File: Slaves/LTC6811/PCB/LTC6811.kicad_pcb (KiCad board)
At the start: 2 copper layers, 100 x 100 mm, 108 parts, among them J1 Cells, J2 Slave, J3 Master, J4 Temperature, J5 Conn_01x01, J6 Conn_01x01, J7 Conn_01x01, J8 Conn_01x01, Q1 NSV1C201MZ4, Q10 TSM2323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

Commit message: description on PCB
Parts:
- added LOGO1: Logo_Open_Hardware_Small, ENNOID:ENNOID-LOGO, B.Cu at (53.0, 39.0)
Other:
- board text added: "LTC6811"
- board text added: "Slave LTC6811 - 01/2018 https://github.com/EnnoidMe/ENNOID-BMS"

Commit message: UPS update
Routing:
- net Net-(F6-Pad1): track 3.71 -> 9.70 mm
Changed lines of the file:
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@@
     (thickness 1.6)
     (drawings 10)
-    (tracks 666)
+    (tracks 667)
     (zones 0)
     (modules 109)
@@
   (segment (start 29 51.05) (end 30.85 51.05) (width 0.25) (layer F.Cu) (net 36) (status 30))
   (segment (start 5.92 46) (end 3.3 48.62) (width 0.25) (layer F.Cu) (net 37) (status 20))
+  (segment (start 5.92 46) (end 11.91 46) (width 0.25) (layer F.Cu) (net 37))
   (segment (start 4.14 52) (end 3.3 51.16) (width 0.25) (layer F.Cu) (net 38) (status 30))
   (segment (start 11.91 52) (end 4.14 52) (width 0.25) (layer F.Cu) (net 38) (status 30))

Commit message: UPS completed
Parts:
- moved J4 0.82 mm to (67.5, 97.5)
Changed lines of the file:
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@@
     (47 F.CrtYd user)
     (48 B.Fab user)
-    (49 F.Fab user)
+    (49 F.Fab user hide)
   )
   (setup
@@
   )
   (module Pin_Headers:Pin_Header_Straight_1x06_Pitch2.54mm (layer F.Cu)
-    (at 67.3 96.7 90)
+    (at 67.5 97.5 90)
     (descr "Through hole straight pin header, 1x06, 2.54mm pitch, single row")
     (tags "Through hole pin header THT 1x06 2.54mm single row")

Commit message: Software added
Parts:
- C13, C14, C15, C16, C17, C18, C19, C20, C21, C22, C23, C24: footprint Capacitors_SMD:C_0603_HandSoldering -> Capacitors_SMD:C_0805_HandSoldering

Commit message: LTC6811 added diode protection inputs
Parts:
- added D1: PDZ7.5B, Diodes_SMD:D_SOD-323_HandSoldering, F.Cu at (35.9, 23.0)
- added D10: PDZ7.5B, Diodes_SMD:D_SOD-323_HandSoldering, F.Cu at (35.9, 77.0)
- added D11: PDZ7.5B, Diodes_SMD:D_SOD-323_HandSoldering, F.Cu at (35.9, 83.3)
- added D12: PDZ7.5B, Diodes_SMD:D_SOD-323_HandSoldering, F.Cu at (35.9, 89.0)
- added D2: PDZ7.5B, Diodes_SMD:D_SOD-323_HandSoldering, F.Cu at (35.9, 29.0)
- added D3: PDZ7.5B, Diodes_SMD:D_SOD-323_HandSoldering, F.Cu at (35.9, 35.0)
- added D4: PDZ7.5B, Diodes_SMD:D_SOD-323_HandSoldering, F.Cu at (35.9, 41.0)
- added D5: PDZ7.5B, Diodes_SMD:D_SOD-323_HandSoldering, F.Cu at (35.9, 47.0)
- added D6: PDZ7.5B, Diodes_SMD:D_SOD-323_HandSoldering, F.Cu at (35.9, 53.0)
- added D7: PDZ7.5B, Diodes_SMD:D_SOD-323_HandSoldering, F.Cu at (35.9, 59.5)
- added D8: PDZ7.5B, Diodes_SMD:D_SOD-323_HandSoldering, F.Cu at (35.9, 65.5)
- added D9: PDZ7.5B, Diodes_SMD:D_SOD-323_HandSoldering, F.Cu at (35.9, 71.0)
- added F13: 0.25A, Fuse_Holders_and_Fuses:Fuse_SMD1206_HandSoldering, F.Cu at (14.0, 88.0)
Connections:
- J1 pad 1: GND -> Net-(F13-Pad1)
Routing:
- net Net-(F13-Pad1): track 0.00 -> 27.2 mm
- net GND: track 96.2 -> 71.4 mm, vias 27 -> 30
- net /cell6/C: track 18.9 -> 24.1 mm
- net /cell7/C: track 18.1 -> 23.1 mm
- net /cell11/C: track 35.2 -> 40.0 mm
- net /cell5/C: track 21.0 -> 25.7 mm
- net /cell9/C: track 25.9 -> 30.6 mm
- net /cell8/C: track 20.1 -> 24.8 mm
- net /cell10/C: track 30.8 -> 35.3 mm
- net /cell2/C: track 38.3 -> 42.6 mm
- net /cell1/C: track 42.7 -> 46.6 mm
- net /cell3/C: track 31.7 -> 35.2 mm
- net /cell4/C: track 26.9 -> 29.9 mm
- net /cell6/S: track 19.5 -> 21.1 mm
- net /cell12/C: track 40.9 -> 42.0 mm
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
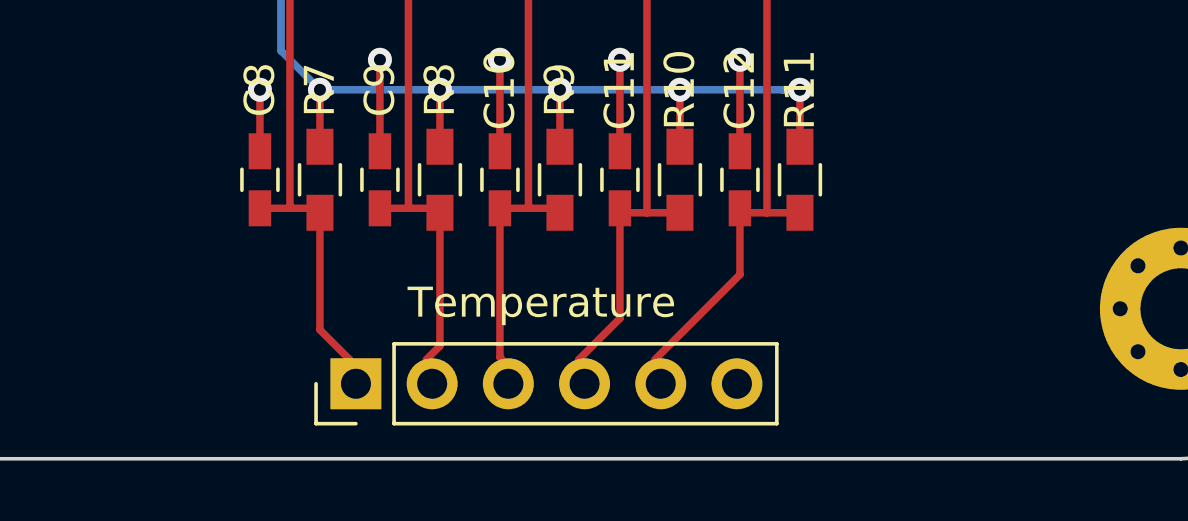
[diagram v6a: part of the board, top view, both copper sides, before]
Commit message: temperatures sensors now has  separate grounds
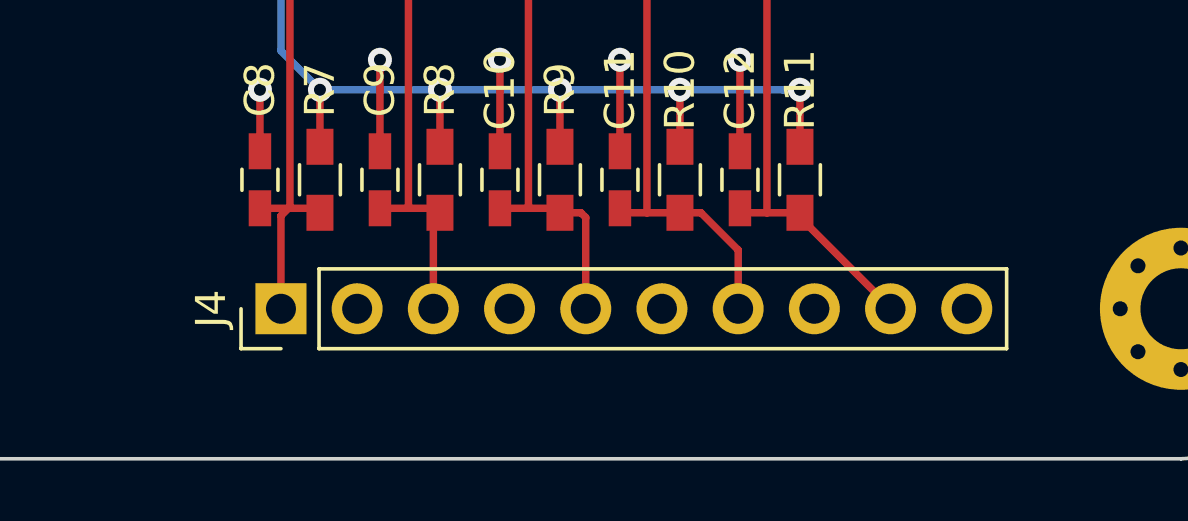
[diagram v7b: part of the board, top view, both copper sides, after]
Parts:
- J4: footprint Pin_Headers:Pin_Header_Straight_1x06_Pitch2.54mm -> Pin_Headers:Pin_Header_Straight_1x10_Pitch2.54mm
- moved J4 3.54 mm to (65.0, 95.0)
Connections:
- J4 pad 2: /T2 -> GND
- J4 pad 3: /T3 -> /T2
- J4 pad 4: /T4 -> GND
- J4 pad 5: /T5 -> /T3
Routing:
- net /T1: track 46.9 -> 45.0 mm
- net /T2: track 49.1 -> 47.3 mm
- net /T5: track 58.2 -> 56.4 mm
- net /T4: track 55.1 -> 53.9 mm
- net /T3: track 51.5 -> 50.4 mm

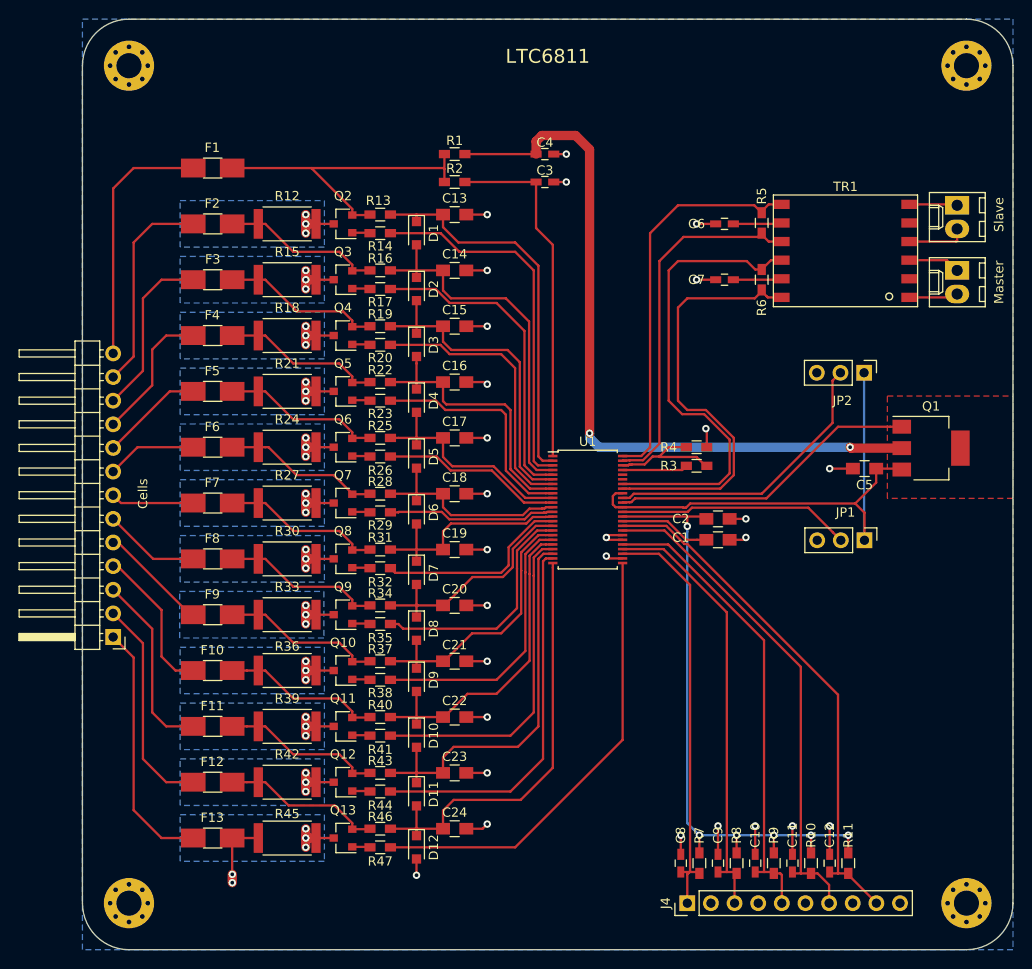
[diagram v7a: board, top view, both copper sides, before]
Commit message: LTC6811 is now 2W per level
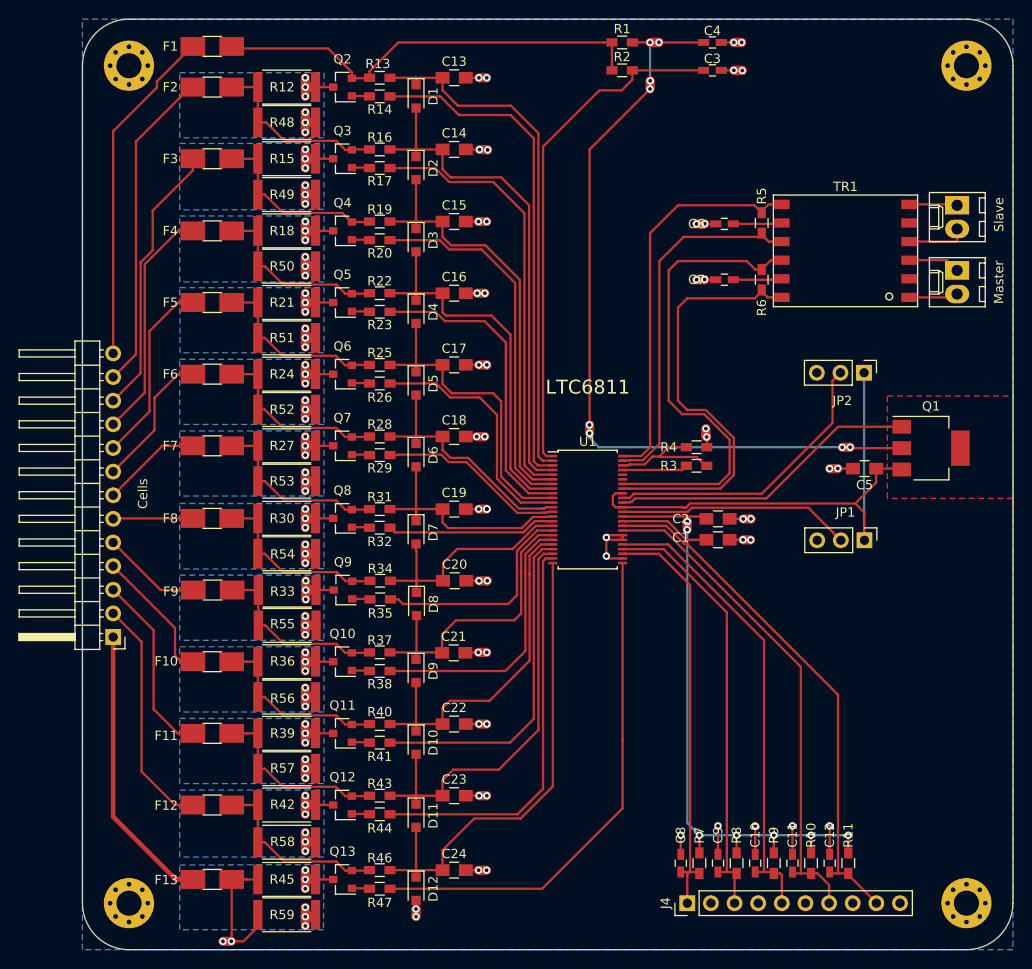
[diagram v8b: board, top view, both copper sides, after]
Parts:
- added R48: 15, Resistors_SMD:R_2512, F.Cu at (21.9, 11.1)
- added R49: 15, Resistors_SMD:R_2512, F.Cu at (21.9, 18.9)
- added R50: 15, Resistors_SMD:R_2512, F.Cu at (21.9, 26.6)
- added R51: 15, Resistors_SMD:R_2512, F.Cu at (21.9, 34.2)
- added R52: 15, Resistors_SMD:R_2512, F.Cu at (21.9, 42.0)
- added R53: 15, Resistors_SMD:R_2512, F.Cu at (21.9, 49.6)
- added R54: 15, Resistors_SMD:R_2512, F.Cu at (21.9, 57.5)
- added R55: 15, Resistors_SMD:R_2512, F.Cu at (22.0, 65.2)
- added R56: 15, Resistors_SMD:R_2512, F.Cu at (21.9, 72.8)
- added R57: 15, Resistors_SMD:R_2512, F.Cu at (21.9, 80.5)
- added R58: 15, Resistors_SMD:R_2512, F.Cu at (21.9, 88.5)
- added R59: 15, Resistors_SMD:R_2512, F.Cu at (21.9, 96.2)
- R12, R15, R18, R21, R24, R27, R30, R33, R36, R39, R42, R45: value 33 -> 15
- moved C3 21.6 mm to (67.7, 5.50)
- moved C4 21.6 mm to (67.7, 2.50)
- moved R1 21.6 mm to (58.0, 2.50)
- moved R2 21.6 mm to (58.0, 5.50)
- moved C13 14.7 mm to (40.0, 6.30)
- moved D1 14.7 mm to (35.9, 8.30)
- moved F2 14.7 mm to (13.9, 7.30)
- moved Q2 14.7 mm to (27.9, 7.30)
- moved R12 14.7 mm to (21.9, 7.30)
- moved R13 14.7 mm to (31.9, 6.30)
- moved R14 14.7 mm to (31.9, 8.30)
- moved F1 13.1 mm to (13.9, 2.92)
- moved C14 13.0 mm to (40.0, 14.0)
- moved D2 13.0 mm to (35.9, 16.0)
- moved F3 13.0 mm to (13.9, 15.0)
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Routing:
- net GND: track 71.4 -> 99.6 mm, vias 30 -> 52
- net Net-(C3-Pad1): track 37.8 -> 55.3 mm
- net /cell12/C: track 42.0 -> 56.4 mm
- net /cell12/S: track 39.8 -> 54.3 mm
- net /cell11/C: track 40.0 -> 54.4 mm
- net /cell12/C+: track 34.6 -> 47.6 mm
- net /cell11/S: track 34.2 -> 47.0 mm
- net /cell10/C: track 35.3 -> 47.7 mm
- net Net-(F2-Pad1): track 22.6 -> 34.8 mm
- net /cell9/C: track 30.6 -> 41.8 mm
- net Net-(F3-Pad1): track 18.6 -> 29.5 mm
- net /cell8/C: track 24.8 -> 35.3 mm
- net Net-(F4-Pad1): track 14.8 -> 25.3 mm
- net /cell10/S: track 29.9 -> 40.0 mm
- net Net-(C4-Pad1): track 80.7 -> 90.4 mm, vias 2 -> 8
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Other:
- net class wide: clearance 1 -> 0.5
